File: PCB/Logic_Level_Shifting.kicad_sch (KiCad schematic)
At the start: 24 parts, among them J3 Conn_01x02_Pin, Q4 BSS123

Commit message: Merging commit
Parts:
- removed Q4 (x4): BSS123, Package_TO_SOT_SMD:SOT-23, symbol Transistor_FET:BSS123
- added Q3, Q4, Q5, Q6: BSS138, Package_TO_SOT_SMD:SOT-23, symbol Transistor_FET:BSS138
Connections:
- net 2V8: now also Q3.1 (G), Q4.1 (G), Q5.1 (G), Q6.1 (G)
- net at R?.2, R?.2: now also Q5.2 (S)
- net at R?.1, R?.2: now also Q5.3 (D)
- net at R?.2, R?.2: now also Q4.2 (S)
- net at R?.1, R?.2: now also Q4.3 (D)
- net at R?.1, R?.2: now also Q3.3 (D)
- net at R?.2, R?.2: now also Q3.2 (S)
- net at R?.2, R?.2: now also Q6.2 (S)
- net at R?.1, R?.2: now also Q6.3 (D)
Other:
- company: (none) -> Univercity of Cape Town
- title: (none) -> Logic Level Shifting

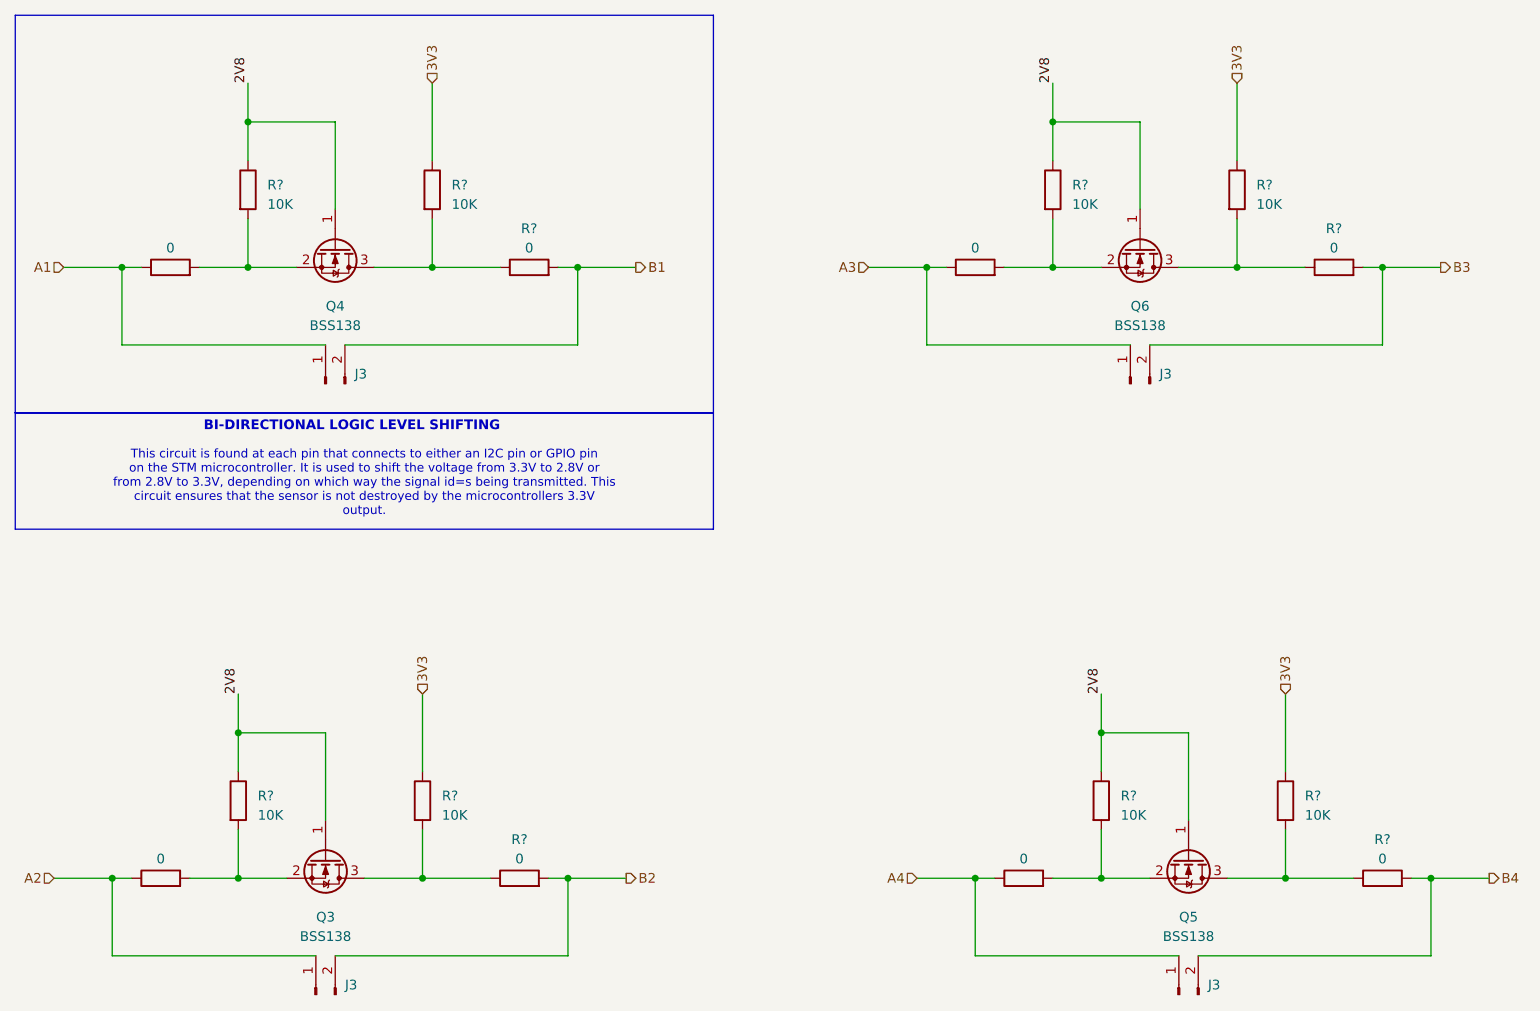
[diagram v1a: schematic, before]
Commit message: commenting of trace thicknesses
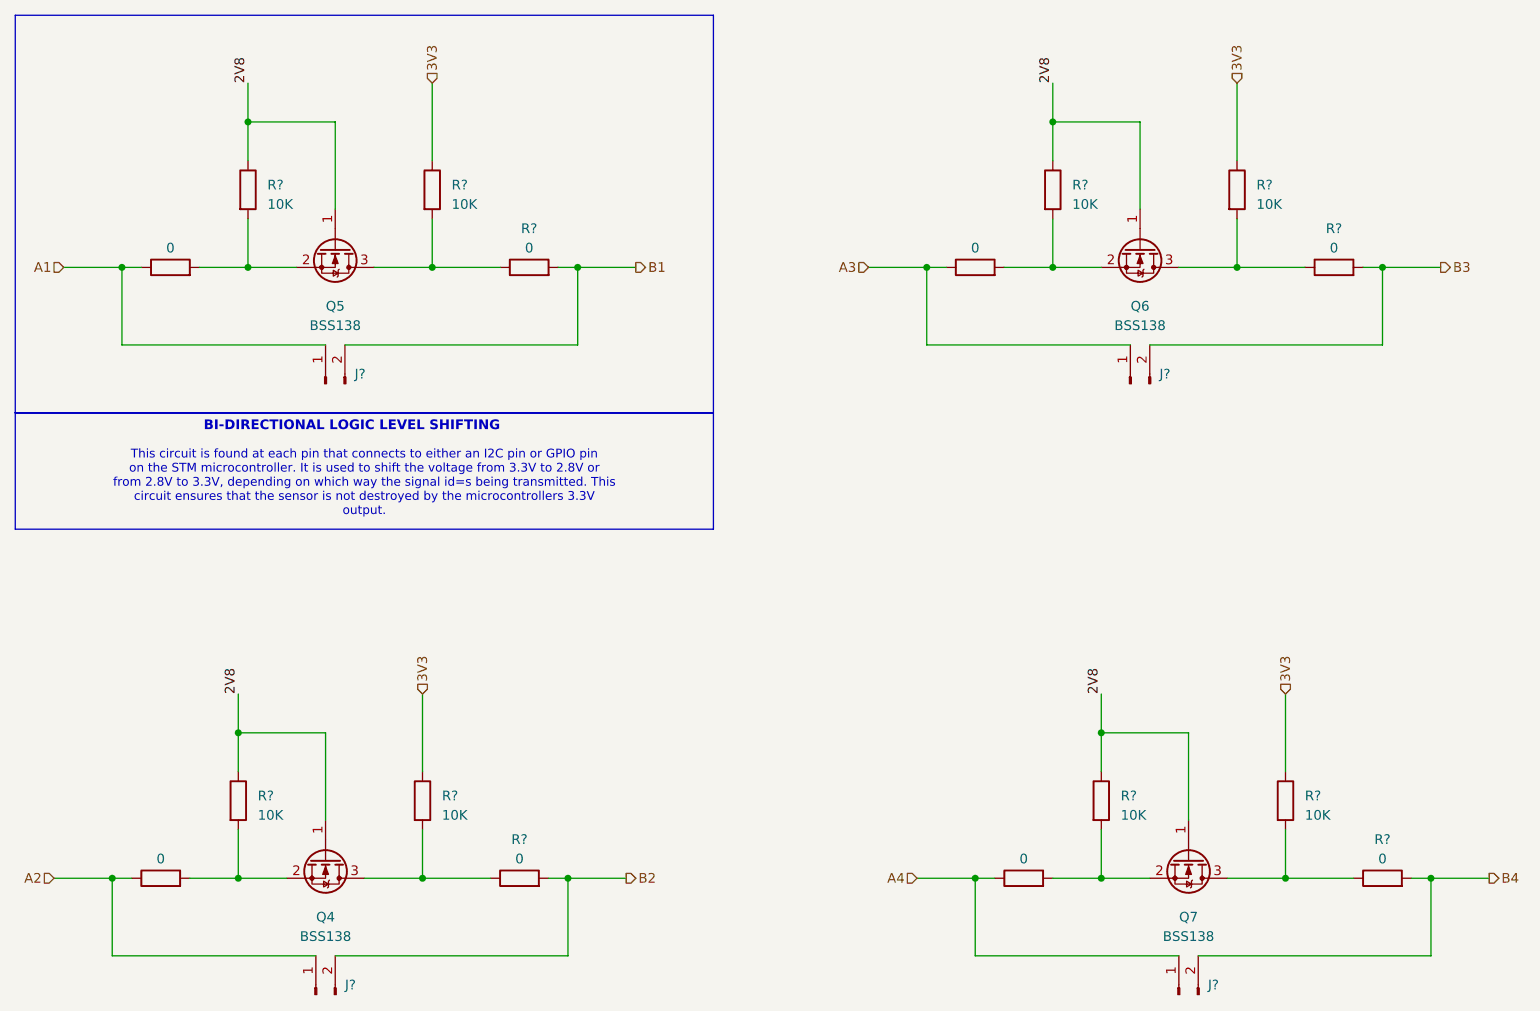
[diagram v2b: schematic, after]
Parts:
- renumbered J3 to J?, Q3 to Q4, Q4 to Q5, Q5 to Q7
